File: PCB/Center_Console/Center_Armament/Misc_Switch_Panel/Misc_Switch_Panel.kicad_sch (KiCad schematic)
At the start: 29 parts, among them J1 MAIN_ARMAMENT_PANEL, J2 SWITCHES, J3 SHRIKE_VOL, J4 LED_BACKLIGHT, U1 MCP23017x-x-SO

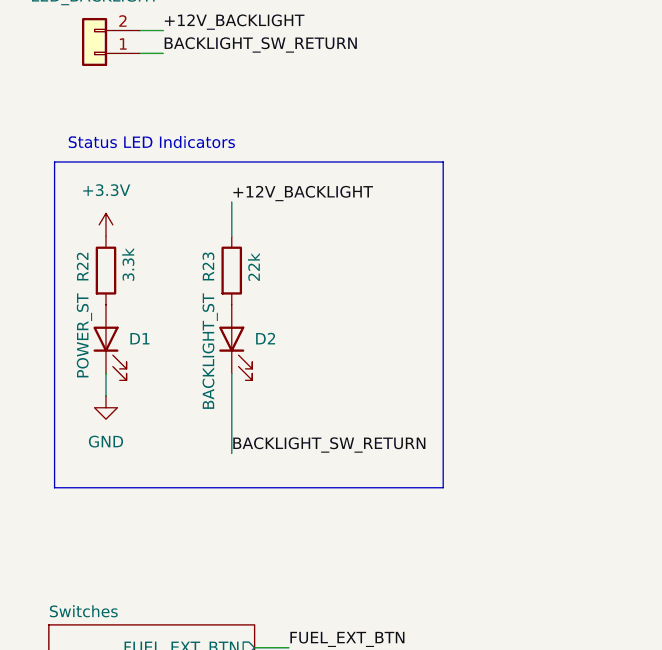
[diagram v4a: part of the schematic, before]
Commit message: Add AWRS_Panel schematic; refresh symbol caches
AWRS_Panel: 2-sheet hierarchical breakout board schematic.
Root sheet: ADS1115 @ 0x48 (ADDR→GND), three RC-filtered analog inputs
(A0=QTY, A1=DROP INTVL, A2=MODE SEL), 1kΩ+100nF per input, three 4-pin
JST-XH pot connectors (J1/J3/J5), 6-pin JST-XH MCU harness (J2), VDD
decoupling (C1 100nF + C2 10µF), status LED (D1+R22), PWR_FLAGs.
Backlighting sheet: 3 LED strings × 5 LEDs, 3×120Ω resistors, 2-pin
Mini-Fit Jr (J_LED). Controls sheet: placeholder — panel-mounted switch
types and position counts deferred until extracted from DCS sim.

MCU_CAN.kicad_sch, Misc_Switch_Panel.kicad_sch: symbol cache refresh
from IRLML2502 library rework.
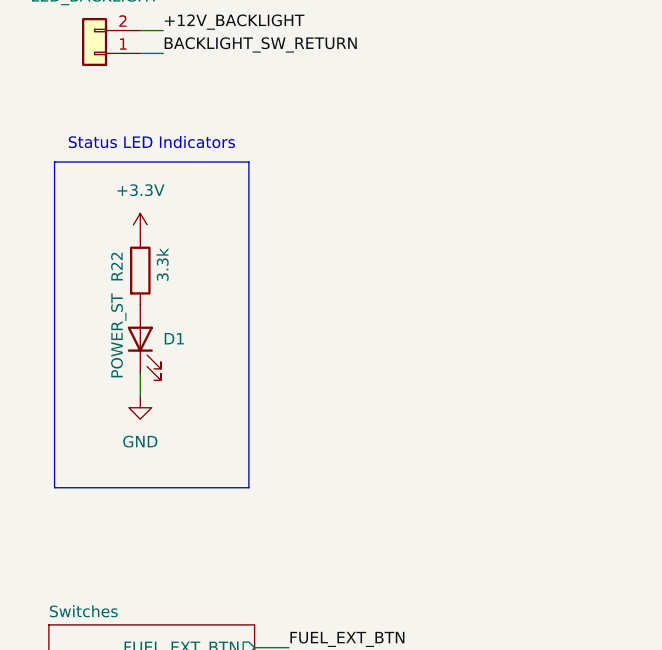
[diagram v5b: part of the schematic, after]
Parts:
- removed D2: BACKLIGHT_ST, LED_SMD:LED_0805_2012Metric, symbol Device:LED
- removed R23: 22k, Capacitor_SMD:C_0805_2012Metric, symbol Device:R
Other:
- moved on the sheet: D1, R22
